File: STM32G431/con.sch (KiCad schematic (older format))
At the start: 61 parts, among them J10 NTC, J11 LED, J4 GND, J5 VIN, J6 UART, J8 HALL, J9 AIN/PWM, P1 TC2030-CTX-Tag-Connect, Q2 Q_NMOS_GSD, U11 USBLC6-4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

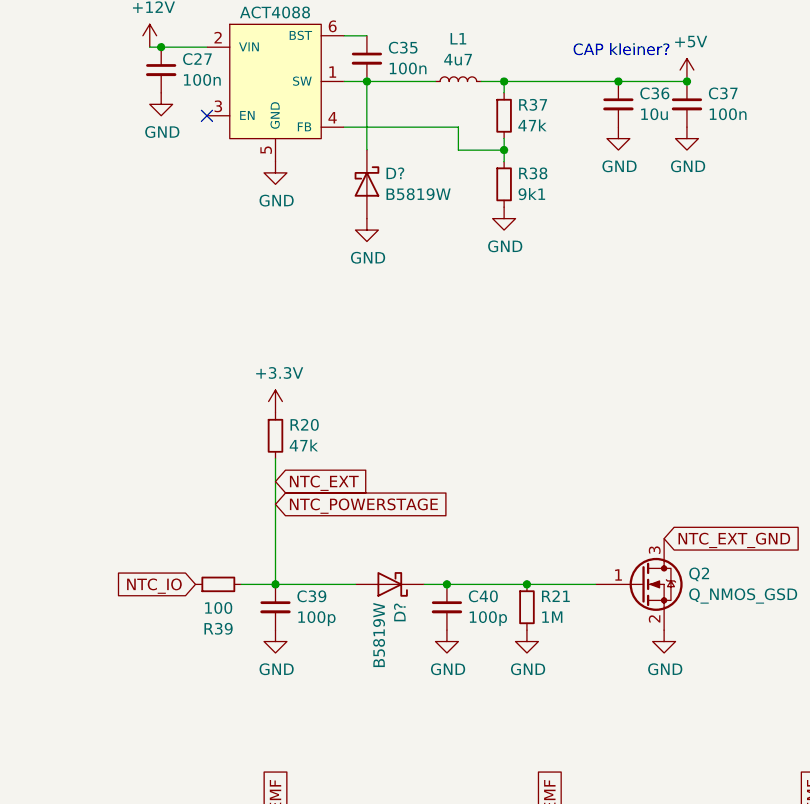
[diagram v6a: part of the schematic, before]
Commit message: updated layout
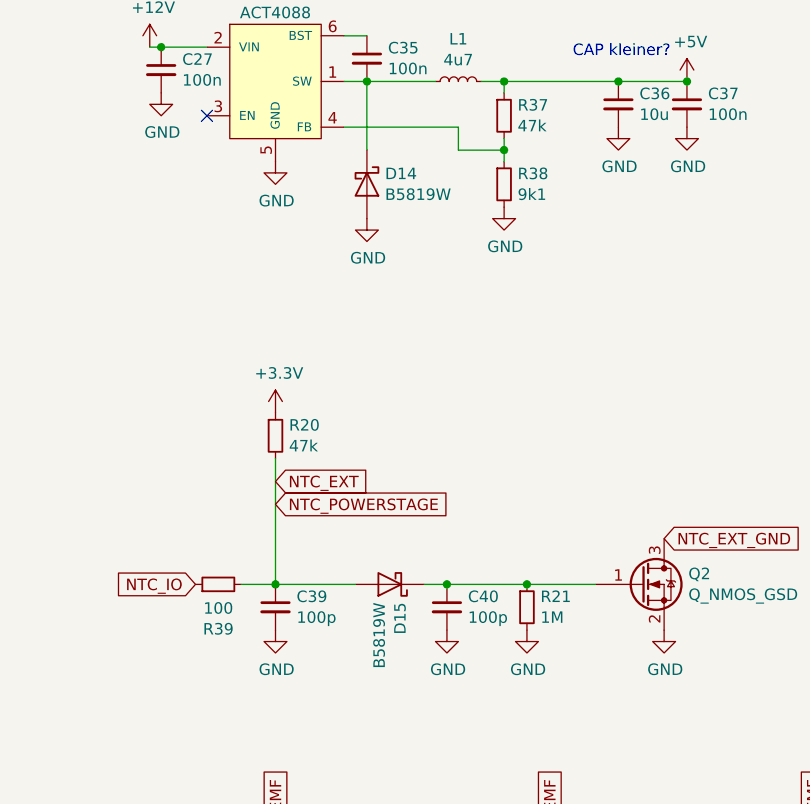
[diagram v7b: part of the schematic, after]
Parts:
- gave numbers to parts that had none: 2
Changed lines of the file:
@@
 $EndComp
 $Comp
-L power:+3.3V #PWR?
+L power:+3.3V #PWR0232
 U 1 1 5E0AF941
 P 4150 4450
-F 0 "#PWR?" H 4150 4300 50  0001 C CNN
+F 0 "#PWR0232" H 4150 4300 50  0001 C CNN
 F 1 "+3.3V" H 4165 4623 50  0000 C CNN
 F 2 "" H 4150 4450 50  0001 C CNN
@@
 	4150 5200 4500 5200
 $Comp
-L Device:D_Schottky D?
+L Device:D_Schottky D15
 U 1 1 5DFB1AE0
 P 4650 5200
-F 0 "D?" V 4604 5279 50  0000 L CNN
+F 0 "D15" V 4604 5279 50  0000 L CNN
 F 1 "B5819W" V 4695 5279 50  0000 L CNN
 F 2 "Diode_SMD:D_SOD-123" H 4650 5200 50  0001 C CNN
@@
 $EndComp
 $Comp
-L Device:D_Schottky D?
+L Device:D_Schottky D14
 U 1 1 5DFBDED8
 P 4550 3450
-F 0 "D?" V 4504 3529 50  0000 L CNN
+F 0 "D14" V 4504 3529 50  0000 L CNN
 F 1 "B5819W" V 4595 3529 50  0000 L CNN
 F 2 "Diode_SMD:D_SOD-123" H 4550 3450 50  0001 C CNN

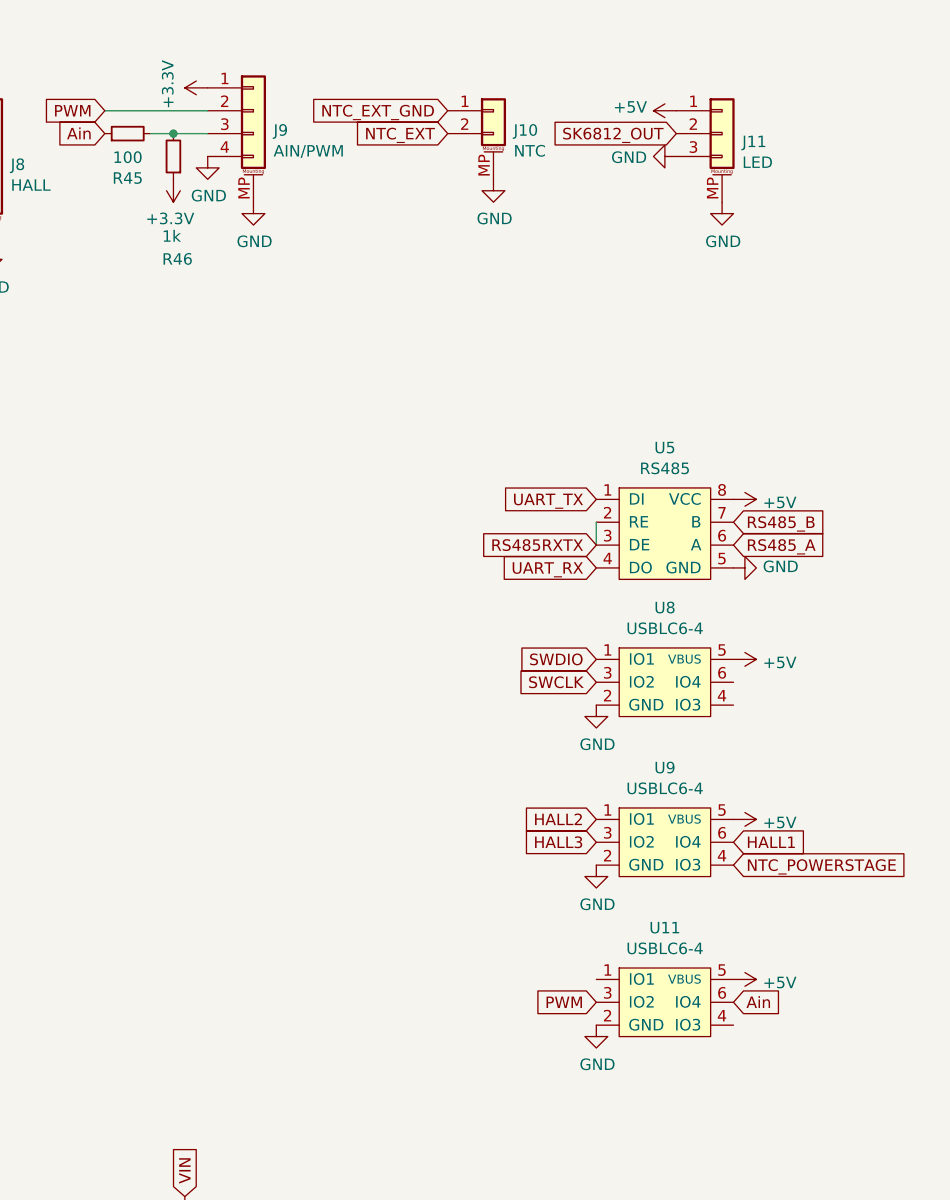
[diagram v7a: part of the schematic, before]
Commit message: updated layout
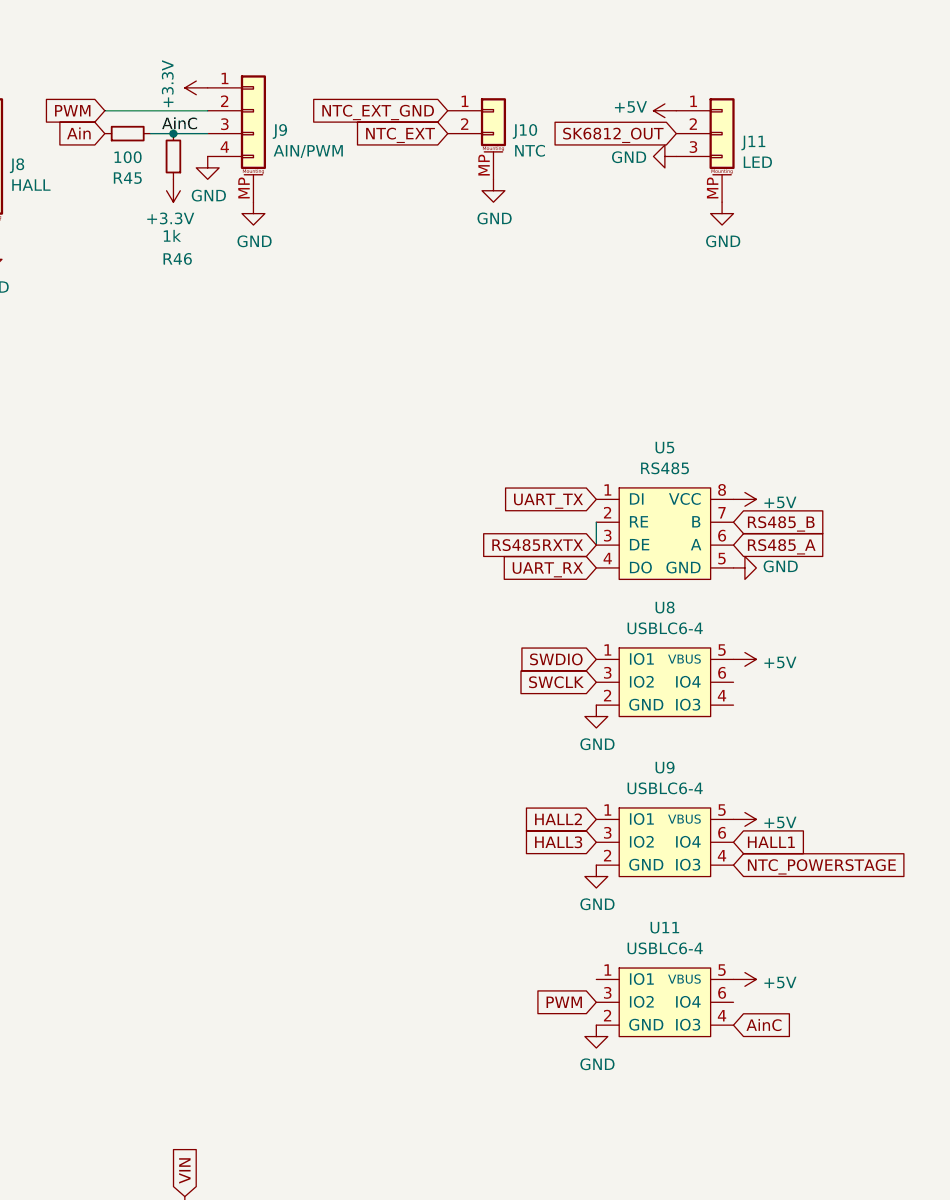
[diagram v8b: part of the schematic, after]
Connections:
- net Ain: no longer U11.6 (IO4)
- net AinC: now reaches J9.3 (Pin_3), R45.2, R46.2
- net AinC: now also U11.4 (IO3)
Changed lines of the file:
@@
 Text GLabel 10150 4300 2    50   Input ~ 0
 NTC_POWERSTAGE
-Text GLabel 10150 4900 2    50   Input ~ 0
-Ain
+Text GLabel 10150 5000 2    50   Input ~ 0
+AinC
 $Comp
 L power:GND #PWR0164
@@
 	0    1    1    0
 $EndComp
+Text Label 7650 1100 0    50   ~ 0
+AinC
 $EndSCHEMATC
